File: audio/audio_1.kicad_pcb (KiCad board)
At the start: 2 copper layers, 24.1 x 36.8 mm, 3 parts, among them J1 Comum, J2 Esquerdo, J3 Direito

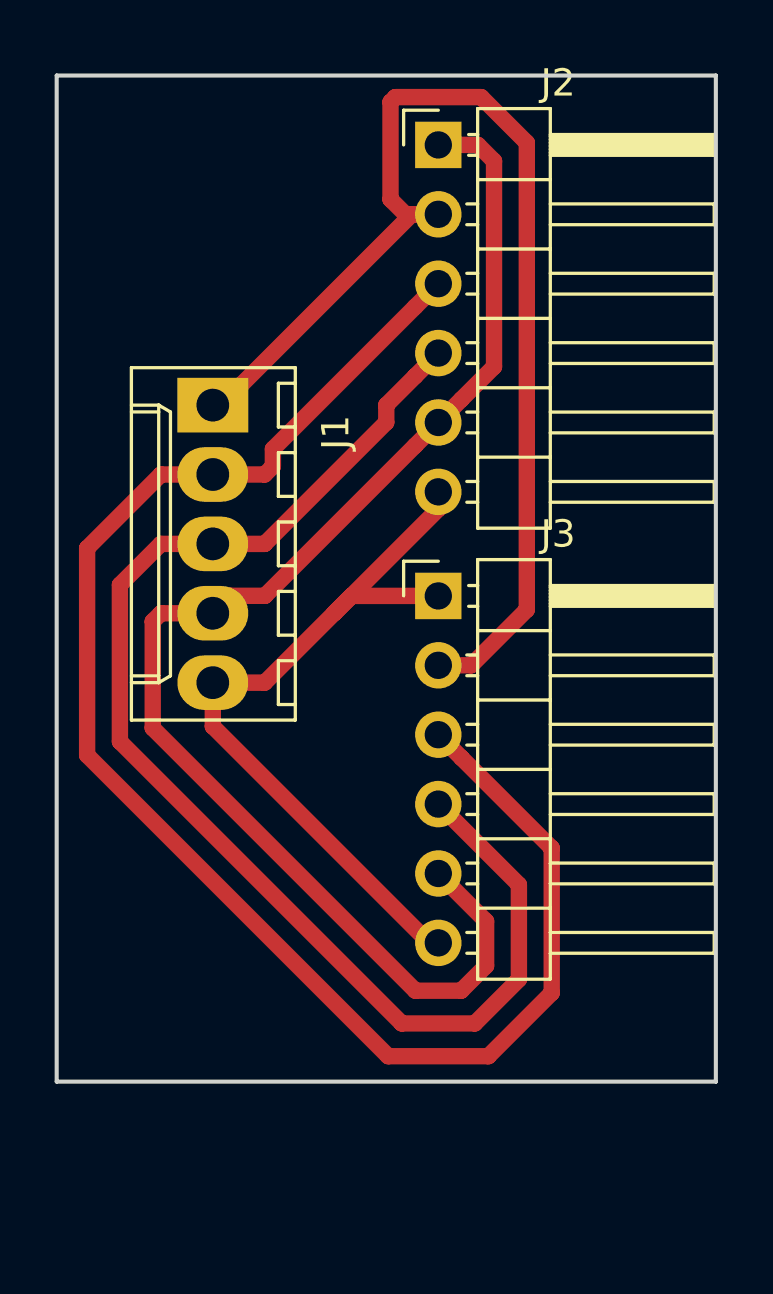
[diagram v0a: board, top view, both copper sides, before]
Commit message: Corrigida alimentação do led, botão e resistor de pull down
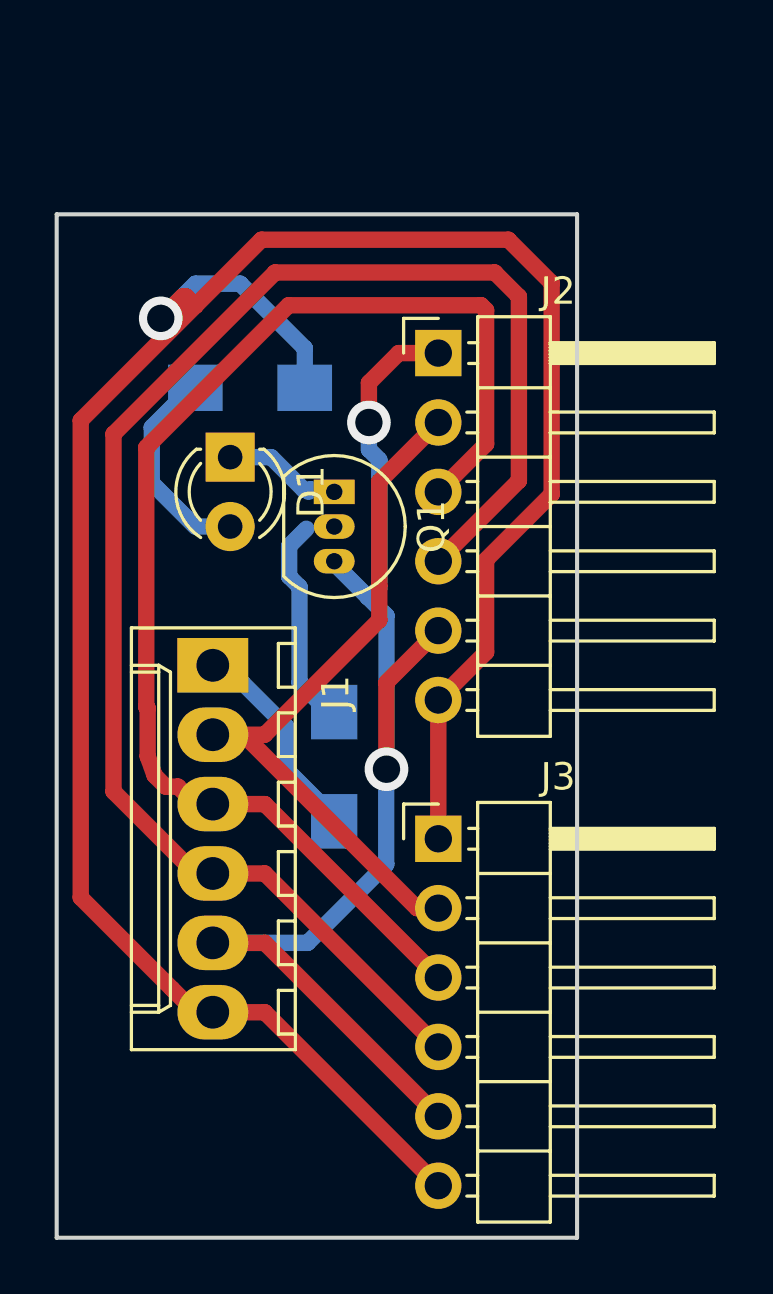
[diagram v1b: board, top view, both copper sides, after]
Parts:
- added D1: LED, LEDs:LED_D3.0mm, F.Cu at (163.8, 99.1)
- added Q1: BC548, TO_SOT_Packages_THT:TO-92_Inline_Narrow_Oval, F.Cu at (167.6, 100.3)
- added R1: 100, Resistors_SMD:R_1206_HandSoldering, B.Cu at (164.6, 96.5)
- added R2: 2700, Resistors_SMD:R_1206_HandSoldering, B.Cu at (167.6, 110.4)
- J1: value Comum -> Conn_01x06; footprint Connectors_Molex:Molex_KK-6410-05_05x2.54mm_Straight -> Connectors_Molex:Molex_KK-6410-06_06x2.54mm_Straight
- moved J1 9.53 mm to (163.2, 106.7)
- moved J3 8.89 mm to (171.4, 113.0)
- moved J2 7.62 mm to (171.4, 95.2)
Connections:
- J1 pad 1: lrcl -> Net-(J1-Pad1)
- J1 pad 2: dout -> lrcl
- J1 pad 3: bclk -> dout
- J1 pad 4: gnd -> bclk
- J1 pad 5: 3.3v -> gnd
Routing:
- net 3.3v: track 28.7 -> 88.1 mm, vias 0 -> 1
- net lrcl: track 43.6 -> 27.5 mm
- net dout: track 58.5 -> 47.8 mm
- net Net-(J1-Pad1): track 0.00 -> 9.27 mm
- net bclk: track 48.5 -> 57.4 mm
- net Net-(Q1-Pad2): track 0.00 -> 7.77 mm
- net Net-(D1-Pad2): track 0.00 -> 7.76 mm
- net Net-(D1-Pad1): track 0.00 -> 4.42 mm
- net gnd: track 50.7 -> 49.2 mm, vias 0 -> 2
- added copper zone on B.Cu, net (none)
- added copper zone on F.Cu, net (none)
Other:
- board size 24.1 x 36.8 mm -> 19.1 x 37.5 mm
- net class Default: via_dia 0.8 -> 1.6; via_drill 0.4 -> 1
